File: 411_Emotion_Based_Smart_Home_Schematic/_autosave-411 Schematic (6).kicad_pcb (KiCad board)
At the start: 2 copper layers, 123 x 48 mm, 25 parts, among them Q1 NSS1C301ET4G, Q2 NSS1C301ET4G, Q3 NSS1C301ET4G, U4 HC-SR04

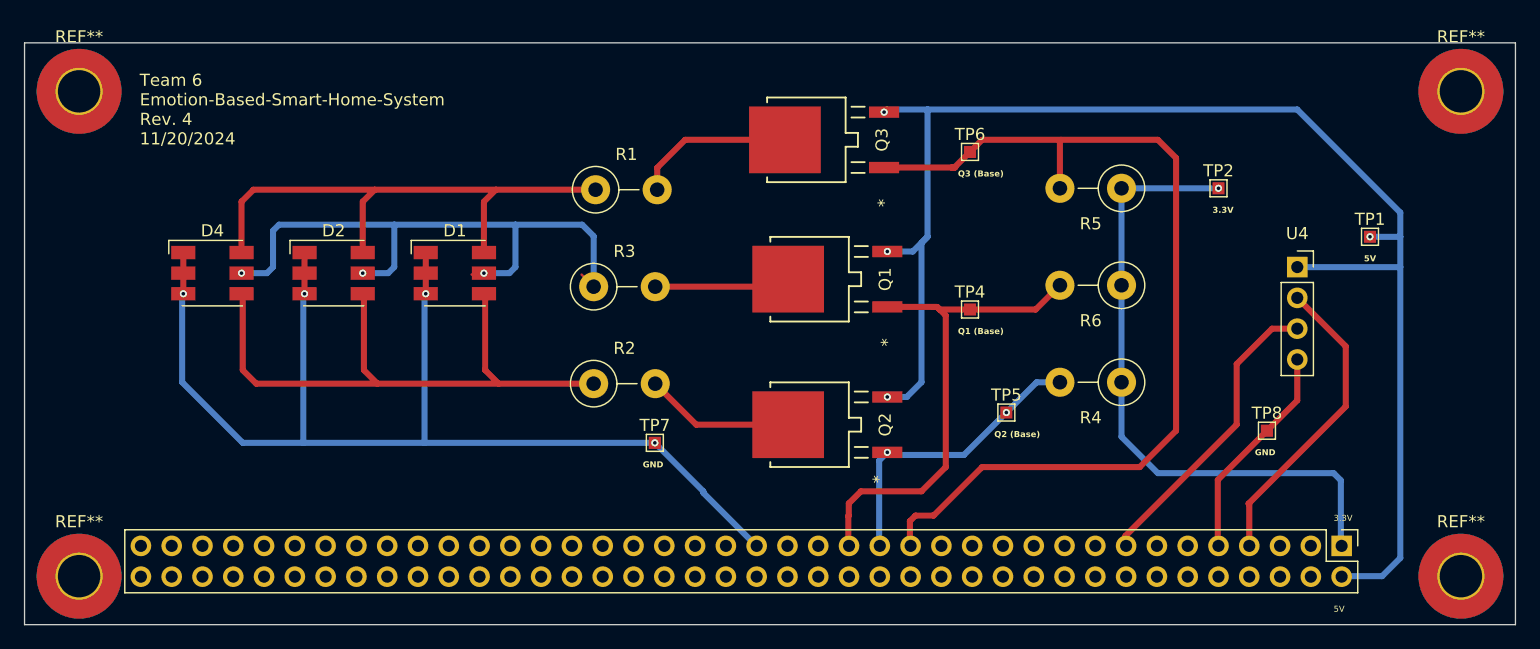
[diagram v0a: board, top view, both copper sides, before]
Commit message: Updated schematic.
Added limiting resistors to each GPIO pins.
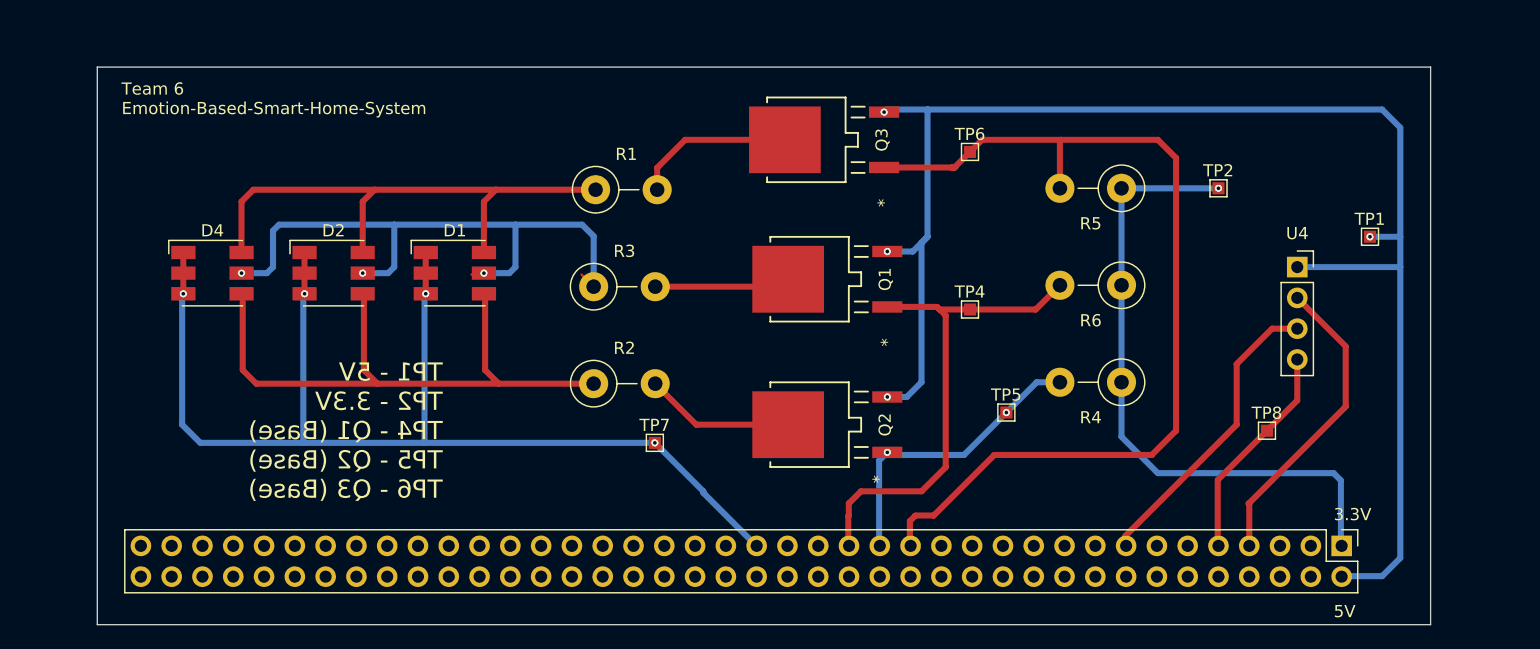
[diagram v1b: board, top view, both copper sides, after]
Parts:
- removed REF** (x4): MountingHole_3.5mm_Pad_TopBottom, MountingHole:MountingHole_3.5mm_Pad_TopBottom
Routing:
- net 5V: track 121.1 -> 125.2 mm
- net GND: track 95.2 -> 97.3 mm
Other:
- board size 123 x 48 mm -> 110 x 46 mm
- board text added: "TP1 - 5V TP2 - 3.3V TP4 - Q1 (Base) TP5 - Q2 (Base) TP6 - Q3 (Base)"
- board text added: "Team 6 Emotion-Based-Smart-Home-System"
- board text removed: "GND"
- board text removed: "Q1 (Base)"
- board text removed: "Q2 (Base)"
- board text removed: "Q3 (Base)"
- board text removed: "Team 6 Emotion-Based-Smart-Home-System Rev. 4 11/20/2024"
